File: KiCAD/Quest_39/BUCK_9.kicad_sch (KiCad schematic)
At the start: 21 parts

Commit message: Fixed most ERC errors
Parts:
- gave numbers to parts that had none: 21
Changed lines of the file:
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@@
   (symbol (lib_id "Device:C") (at 113.03 46.99 0) (unit 1)
     (in_bom yes) (on_board yes) (fields_autoplaced)
-    (property "Reference" "C?" (id 0) (at 116.84 45.7199 0)
+    (property "Reference" "C127" (id 0) (at 116.84 45.7199 0)
       (effects (font (size 1.27 1.27)) (justify left))
     )
@@
   (symbol (lib_id "Device:R") (at 322.58 215.9 0) (unit 1)
     (in_bom yes) (on_board yes) (fields_autoplaced)
-    (property "Reference" "R?" (id 0) (at 325.12 214.6299 0)
+    (property "Reference" "R57" (id 0) (at 325.12 214.6299 0)
       (effects (font (size 1.27 1.27)) (justify left))
     )
@@
   (symbol (lib_id "Device:C") (at 100.33 46.99 0) (unit 1)
     (in_bom yes) (on_board yes) (fields_autoplaced)
-    (property "Reference" "C?" (id 0) (at 104.14 45.7199 0)
+    (property "Reference" "C126" (id 0) (at 104.14 45.7199 0)
       (effects (font (size 1.27 1.27)) (justify left))
     )
@@
   (symbol (lib_id "Device:R") (at 60.96 49.53 0) (unit 1)
     (in_bom yes) (on_board yes) (fields_autoplaced)
-    (property "Reference" "R?" (id 0) (at 63.5 48.2599 0)
+    (property "Reference" "R55" (id 0) (at 63.5 48.2599 0)
       (effects (font (size 1.27 1.27)) (justify left))
     )
@@
   (symbol (lib_id "Device:R") (at 48.26 49.53 0) (unit 1)
     (in_bom yes) (on_board yes) (fields_autoplaced)
-    (property "Reference" "R?" (id 0) (at 50.8 48.2599 0)
+    (property "Reference" "R54" (id 0) (at 50.8 48.2599 0)
       (effects (font (size 1.27 1.27)) (justify left))
     )
@@
   (symbol (lib_id "Device:C_Polarized") (at 368.3 172.72 0) (unit 1)
     (in_bom yes) (on_board yes)
-    (property "Reference" "C?" (id 0) (at 372.0895 171.4075 0)
+    (property "Reference" "C133" (id 0) (at 372.0895 171.4075 0)
       (effects (font (size 1.27 1.27)) (justify left))
     )
@@
   (symbol (lib_id "MCP4151:MCP4151-502E{slash}SN") (at 254 220.98 0) (unit 1)
     (in_bom yes) (on_board yes)
-    (property "Reference" "U?" (id 0) (at 312.42 214.63 0)
+    (property "Reference" "U43" (id 0) (at 312.42 214.63 0)
       (effects (font (size 1.524 1.524)))
     )
@@
   (symbol (lib_id "LTM4611EV:LTM4611EV-PBF") (at 132.08 102.87 0) (unit 1)
     (in_bom yes) (on_board yes)
-    (property "Reference" "U?" (id 0) (at 308.61 50.8 0)
+    (property "Reference" "U42" (id 0) (at 308.61 50.8 0)
       (effects (font (size 1.524 1.524)))
     )
@@
   (symbol (lib_id "Device:C_Polarized") (at 86.36 46.99 0) (unit 1)
     (in_bom yes) (on_board yes) (fields_autoplaced)
-    (property "Reference" "C?" (id 0) (at 90.17 44.8309 0)
+    (property "Reference" "C125" (id 0) (at 90.17 44.8309 0)
       (effects (font (size 1.27 1.27)) (justify left))
     )
@@
   (symbol (lib_id "Device:C_Polarized") (at 381 172.72 0) (unit 1)
     (in_bom yes) (on_board yes)
-    (property "Reference" "C?" (id 0) (at 384.7895 171.4075 0)
+    (property "Reference" "C134" (id 0) (at 384.7895 171.4075 0)
       (effects (font (size 1.27 1.27)) (justify left))
     )
@@
   (symbol (lib_id "Analog_ADC:INA226") (at 78.74 73.66 0) (unit 1)
     (in_bom yes) (on_board yes)
-    (property "Reference" "U?" (id 0) (at 83.82 62.23 0)
+    (property "Reference" "U41" (id 0) (at 83.82 62.23 0)
       (effects (font (size 1.27 1.27)) (justify left))
     )
@@
   (symbol (lib_id "Device:C") (at 337.82 224.79 0) (unit 1)
     (in_bom yes) (on_board yes) (fields_autoplaced)
-    (property "Reference" "C?" (id 0) (at 341.63 223.5199 0)
+    (property "Reference" "C136" (id 0) (at 341.63 223.5199 0)
       (effects (font (size 1.27 1.27)) (justify left))
     )
@@
   (symbol (lib_id "Amplifier_Operational:MCP601-xOT") (at 35.56 66.04 0) (unit 1)
     (in_bom yes) (on_board yes)
-    (property "Reference" "U?" (id 0) (at 38.1 62.23 0))
+    (property "Reference" "U40" (id 0) (at 38.1 62.23 0))
     (property "Value" "MCP601T-I/OT" (id 1) (at 41.91 69.85 0))
     (property "Footprint" "Package_TO_SOT_SMD:SOT-23-5" (id 2) (at 33.02 71.12 0)
@@
   (symbol (lib_id "Device:C_Polarized") (at 393.7 172.72 0) (unit 1)
     (in_bom yes) (on_board yes)
-    (property "Reference" "C?" (id 0) (at 397.4895 171.4075 0)
+    (property "Reference" "C135" (id 0) (at 397.4895 171.4075 0)
       (effects (font (size 1.27 1.27)) (justify left))
     )
@@
   (symbol (lib_id "Device:C") (at 335.28 172.72 0) (unit 1)
     (in_bom yes) (on_board yes) (fields_autoplaced)
-    (property "Reference" "C?" (id 0) (at 339.09 171.4499 0)
+    (property "Reference" "C131" (id 0) (at 339.09 171.4499 0)
       (effects (font (size 1.27 1.27)) (justify left))
     )
@@
   (symbol (lib_id "Device:R") (at 55.88 41.91 90) (unit 1)
     (in_bom yes) (on_board yes) (fields_autoplaced)
-    (property "Reference" "R?" (id 0) (at 55.88 35.56 90))
+    (property "Reference" "R53" (id 0) (at 55.88 35.56 90))
     (property "Value" "0R0025" (id 1) (at 55.88 38.1 90))
     (property "Footprint" "" (id 2) (at 55.88 43.688 90)
@@
   (symbol (lib_id "Device:C_Polarized") (at 354.33 172.72 0) (unit 1)
     (in_bom yes) (on_board yes)
-    (property "Reference" "C?" (id 0) (at 358.1195 171.4075 0)
+    (property "Reference" "C132" (id 0) (at 358.1195 171.4075 0)
       (effects (font (size 1.27 1.27)) (justify left))
     )
@@
   (symbol (lib_id "Device:R") (at 127 91.44 0) (unit 1)
     (in_bom yes) (on_board yes) (fields_autoplaced)
-    (property "Reference" "R?" (id 0) (at 129.54 90.1699 0)
+    (property "Reference" "R56" (id 0) (at 129.54 90.1699 0)
       (effects (font (size 1.27 1.27)) (justify left))
     )
@@
   (symbol (lib_id "Device:C") (at 125.73 46.99 0) (unit 1)
     (in_bom yes) (on_board yes) (fields_autoplaced)
-    (property "Reference" "C?" (id 0) (at 129.54 45.7199 0)
+    (property "Reference" "C128" (id 0) (at 129.54 45.7199 0)
       (effects (font (size 1.27 1.27)) (justify left))
     )
@@
   (symbol (lib_id "Device:C") (at 128.27 137.16 0) (unit 1)
     (in_bom yes) (on_board yes) (fields_autoplaced)
-    (property "Reference" "C?" (id 0) (at 132.08 135.8899 0)
+    (property "Reference" "C130" (id 0) (at 132.08 135.8899 0)
       (effects (font (size 1.27 1.27)) (justify left))
     )
@@
   (symbol (lib_id "Device:C") (at 55.88 55.88 90) (unit 1)
     (in_bom yes) (on_board yes)
-    (property "Reference" "C?" (id 0) (at 55.88 52.07 90))
+    (property "Reference" "C129" (id 0) (at 55.88 52.07 90))
     (property "Value" "1uF" (id 1) (at 55.88 59.69 90))
     (property "Footprint" "OptoDevice:R_LDR_4.9x4.2mm_P2.54mm_Vertical" (id 2) (at 59.69 54.9148 0)

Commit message: Gave all INA226's unique addresses
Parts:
- removed C125: 330uF, symbol Device:C_Polarized
- removed C126, C127, C128: 22uF, symbol Device:C
- removed C129: 1uF, OptoDevice:R_LDR_4.9x4.2mm_P2.54mm_Vertical, symbol Device:C
- removed C130, C136: 100nF, symbol Device:C
- removed C131: 100pF, symbol Device:C
- removed C132, C133, C134, C135: 100uF, symbol Device:C_Polarized
- removed R53: 0R0025, symbol Device:R
- removed R54, R55: 10, symbol Device:R
- removed R56: 10K, symbol Device:R
- removed R57: 20K, symbol Device:R
- removed U40: MCP601T-I/OT, Package_TO_SOT_SMD:SOT-23-5, symbol Amplifier_Operational:MCP601-xOT
- added C140: 330uF, symbol Device:C_Polarized
- added C141, C142, C143: 22uF, symbol Device:C
- added C144: 1uF, OptoDevice:R_LDR_4.9x4.2mm_P2.54mm_Vertical, symbol Device:C
- added C145, C146, C153: 100nF, symbol Device:C
- added C147: 10nF, symbol Device:C
- added C148, C149, C150, C151: 100uF, symbol Device:C_Polarized
- added C152: 100pF, symbol Device:C
- added R80: 0R0025, symbol Device:R
- added R81, R82: 10R, symbol Device:R
- added R83: 9k, symbol Device:R
- added R84: 1k, symbol Device:R
- added R85: 10k, symbol Device:R
- added R86: 20K, symbol Device:R
- added TP69, TP70, TP71, TP72, TP73, TP74, TP75: TestPoint, symbol Connector:TestPoint
- added U40: AD626ANZ, N_8_ADI, symbol AD626ANZ:AD626ANZ
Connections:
- net +5V: now also U41.2 (A0), C146.1, C153.1, U40.6 (+VS)
- net GND: now also C145.2, C146.2, C153.2, U40.2 (AGND), U40.3 (-VS); no longer U41.1 (A1), U41.2 (A0), U41.3 (~{Alert})
- net NEG: now also C140.2, C141.2, C142.2, C143.2, C147.1, C148.2, C149.2, C150.2, C151.2, R84.2, U40.1 (-IN); no longer U41.8 (Vbus)
- net P0A: now also R86.2
- net POS: now also C148.1, C149.1, C150.1, C151.1, C152.1
- net PV_POS: now also U42.A1 (VIN), U42.A2 (VIN), U42.A3 (VIN), U42.A4 (VIN), U42.A5 (VIN), U42.A6 (VIN), U42.B1 (VIN), U42.B2 (VIN), U42.B3 (VIN), U42.B4 (VIN), U42.B5 (VIN), U42.B6 (VIN), U42.C1 (VIN), U42.C2 (VIN), U42.C3 (VIN), U42.C4 (VIN), U42.C5 (VIN), U42.C6 (VIN), C140.1, C141.1, C142.1, C143.1, R80.1, R80.2, R81.1, R82.1, R83.1, R85.1
- net RUN: now also R85.2
- net SDA: now also U41.1 (A1)
- net TRACK/SS: now also C147.2
- net Vfb: now also C152.2, R86.1
- net Vin+: now also C144.1, R81.2
- net Vin-: now also U41.8 (Vbus), U41.9 (Vin-), C144.2, R82.2, TP70.1, U40.5 (OUT)
- net at U42.A11 (COMP): now also TP73.1
- net at U42.A7 (INTVCC): now also U42.D9 (INTVCC), TP69.1
- net at U42.B12 (PLLFLTR/FSET): now also TP72.1
- net at U42.F11 (PGOOD): now also U42.G12 (PGOOD), TP71.1
- net at U42.K12 (DIFFVOUT), U42.L12 (VOUT_LCL): now also TP74.1, TP75.1
- new net: C145.1, U40.4 (FILTER)
- new net +IN: R83.2, R84.1, U40.8 (+IN)
- no-connect marks 16 -> 12
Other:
- note added: "10:1 divider"
- note added: "Addr=0x49"
- note added: "Extra mounting"
- note added: "G=10"
- note added: "Output voltage is set by varying Rfb with a digipot. SPI = 00"
- note added: "the measured voltage is divided and then amplified by 10 as to simulate a follower. This is done to make use of the AD626 (low price and availability)."

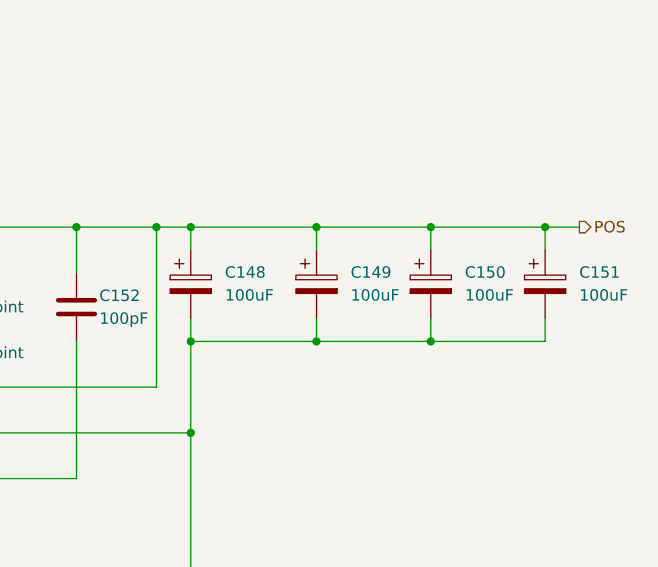
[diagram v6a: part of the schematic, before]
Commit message: Assigned all schem. symbols their footprints
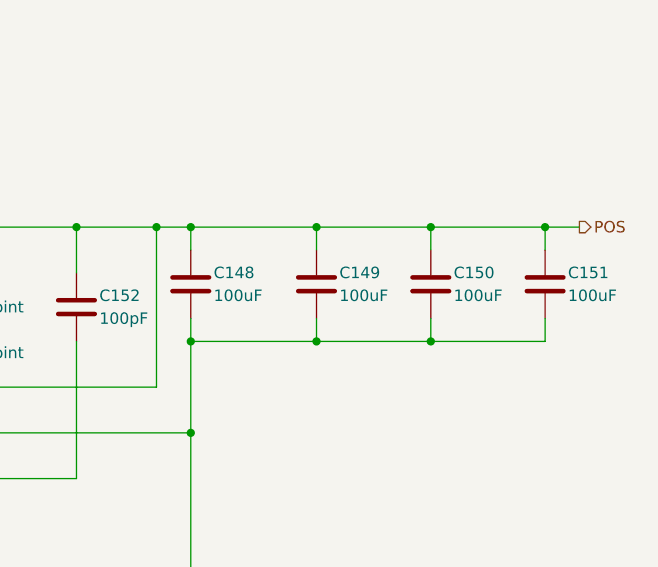
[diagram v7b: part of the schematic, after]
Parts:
- removed C148, C149, C150, C151: 100uF, symbol Device:C_Polarized
- added C148, C149, C150, C151: 100uF, Capacitor_SMD:C_1206_3216Metric, symbol Device:C
- C140: footprint (none) -> Capacitor_SMD:CP_Elec_8x6.9
- C141, C142, C143, C145, C146, C147, C152, C153: footprint (none) -> Capacitor_SMD:C_0805_2012Metric
- C144: footprint OptoDevice:R_LDR_4.9x4.2mm_P2.54mm_Vertical -> Capacitor_SMD:C_0805_2012Metric
- R80: footprint (none) -> Resistor_SMD:R_1206_3216Metric
- R81, R82, R83, R84, R85, R86: footprint (none) -> Resistor_SMD:R_0805_2012Metric
- TP69, TP70, TP71, TP72, TP73, TP74, TP75: footprint (none) -> TestPoint:TestPoint_Pad_D2.0mm
- U40: footprint N_8_ADI -> Package_DIP:DIP-8_W8.89mm_SMDSocket_LongPads
- U42: footprint LGA-133_3_LIT -> Package_LGA:Linear_LGA-133_15.0x15.0mm_Layout12x12_P1.27mm
- U43: footprint SOIC8-N_MC_MCH -> Package_SO:MSOP-8_3x3mm_P0.65mm
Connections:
- net NEG: now also C148.2, C149.2, C150.2, C151.2
- net POS: now also C148.1, C149.1, C150.1, C151.1

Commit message: Initial work on layout
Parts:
- C144, C145, C146, C147, C152, C153: footprint Capacitor_SMD:C_0805_2012Metric -> Capacitor_SMD:C_0603_1608Metric
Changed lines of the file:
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@@
     (property "Reference" "C144" (id 0) (at 74.93 57.15 90))
     (property "Value" "1uF" (id 1) (at 74.93 64.77 90))
-    (property "Footprint" "Capacitor_SMD:C_0805_2012Metric" (id 2) (at 78.74 59.9948 0)
+    (property "Footprint" "Capacitor_SMD:C_0603_1608Metric" (id 2) (at 78.74 59.9948 0)
       (effects (font (size 1.27 1.27)) hide)
     )
@@
       (effects (font (size 1.27 1.27)) (justify left))
     )
-    (property "Footprint" "Capacitor_SMD:C_0805_2012Metric" (id 2) (at 26.3652 81.28 0)
+    (property "Footprint" "Capacitor_SMD:C_0603_1608Metric" (id 2) (at 26.3652 81.28 0)
       (effects (font (size 1.27 1.27)) hide)
     )
@@
       (effects (font (size 1.27 1.27)) (justify left))
     )
-    (property "Footprint" "Capacitor_SMD:C_0805_2012Metric" (id 2) (at 341.3252 220.98 0)
+    (property "Footprint" "Capacitor_SMD:C_0603_1608Metric" (id 2) (at 341.3252 220.98 0)
       (effects (font (size 1.27 1.27)) hide)
     )
@@
       (effects (font (size 1.27 1.27)) (justify left))
     )
-    (property "Footprint" "Capacitor_SMD:C_0805_2012Metric" (id 2) (at 64.4652 82.55 0)
+    (property "Footprint" "Capacitor_SMD:C_0603_1608Metric" (id 2) (at 64.4652 82.55 0)
       (effects (font (size 1.27 1.27)) hide)
     )
@@
       (effects (font (size 1.27 1.27)) (justify left))
     )
-    (property "Footprint" "Capacitor_SMD:C_0805_2012Metric" (id 2) (at 106.3752 124.46 0)
+    (property "Footprint" "Capacitor_SMD:C_0603_1608Metric" (id 2) (at 106.3752 124.46 0)
       (effects (font (size 1.27 1.27)) hide)
     )
@@
       (effects (font (size 1.27 1.27)) (justify left))
     )
-    (property "Footprint" "Capacitor_SMD:C_0805_2012Metric" (id 2) (at 345.1352 168.91 0)
-      (effects (font (size 1.27 1.27)) hide)
-    )
+    (property "Footprint" "Capacitor_SMD:C_0603_1608Metric" (id 2) (at 345.1352 168.91 0)
+      (effects (font (size 1.27 1.27)) hide)
+    )
